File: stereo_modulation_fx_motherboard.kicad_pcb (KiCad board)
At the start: 2 copper layers, 101.6 x 139.7 mm, 87 parts, among them J1 dry_out_A, J10 Conn_01x04_Male, J11 Conn_01x04_Male, J12 Conn_01x04_Male, J13 Conn_01x02_Male, J14 Conn_01x02_Male, J2 CV_out_A, J3 wet_in_A, J4 rez_CV_out_A, J5 dry_out_B, J6 CV_out_B, J7 wet_in_B, J8 rez_CV_out_B, SW1 sweep_mode, SW2 invert_B, SW3 DPDT_on_on_on, U1 Teensy3.2, U10 DG419LDY, U11 DG419LDY, U2 CD74HC4067M, U3 MCP4822, U4 MCP4822, U5 TL072, U6 MCP6002-xSN, U7 TL072, U8 MCP6002-xSN, U9 CC3-0512DF-E

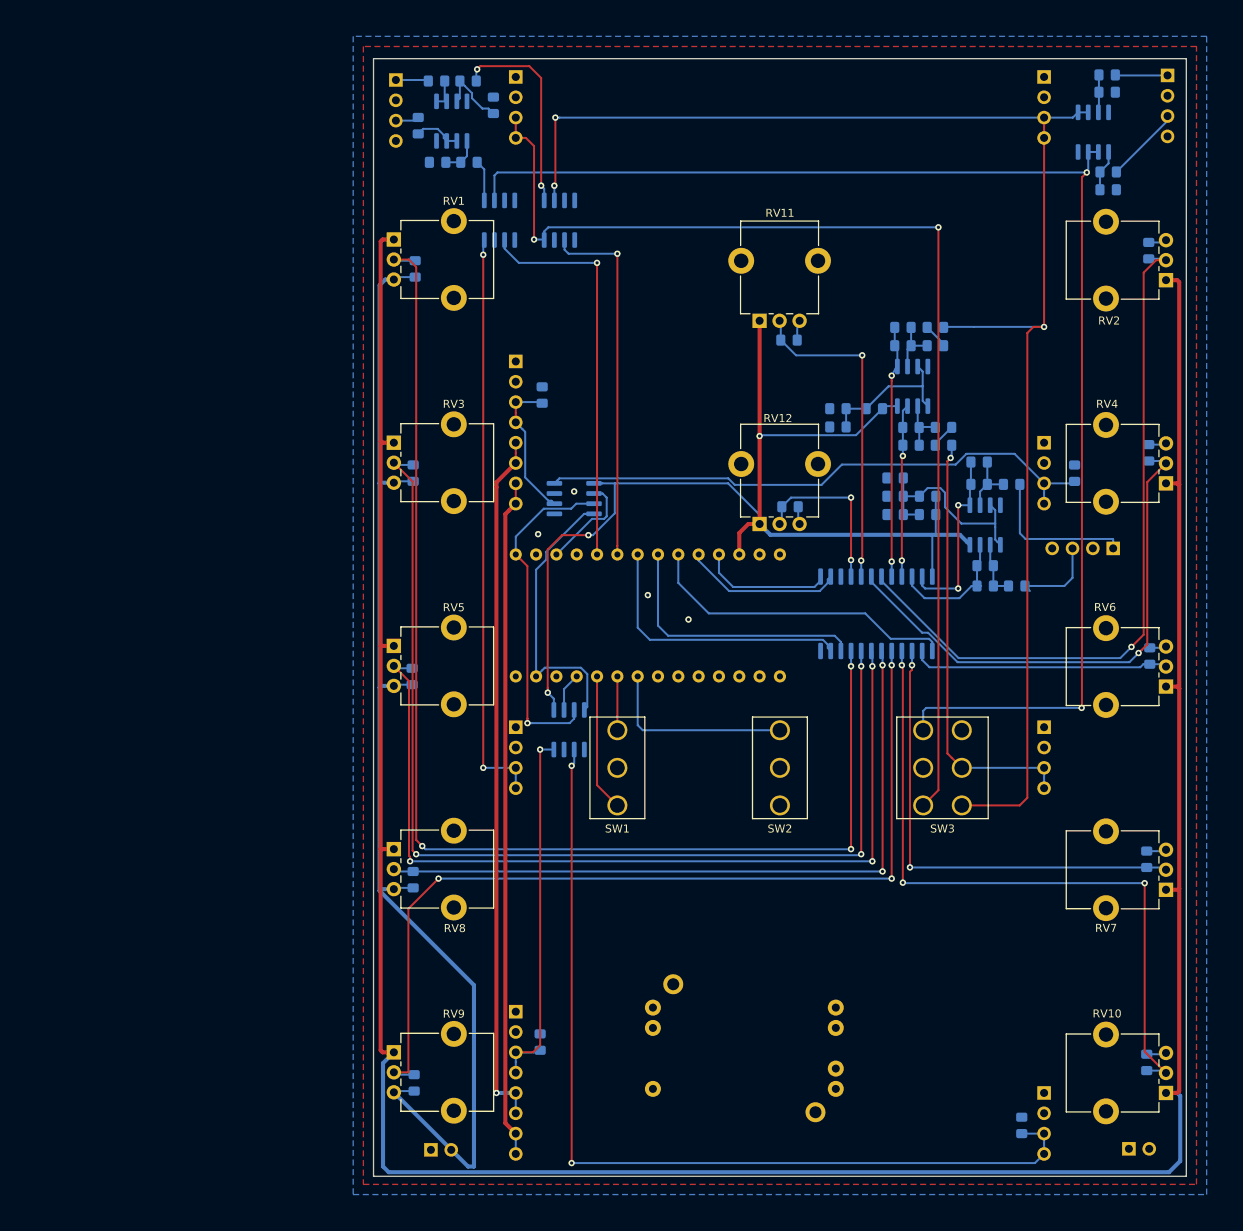
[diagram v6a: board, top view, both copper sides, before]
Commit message: move traces/vias away from pot tabs, progress on routing, NOT DONEgit add -A!
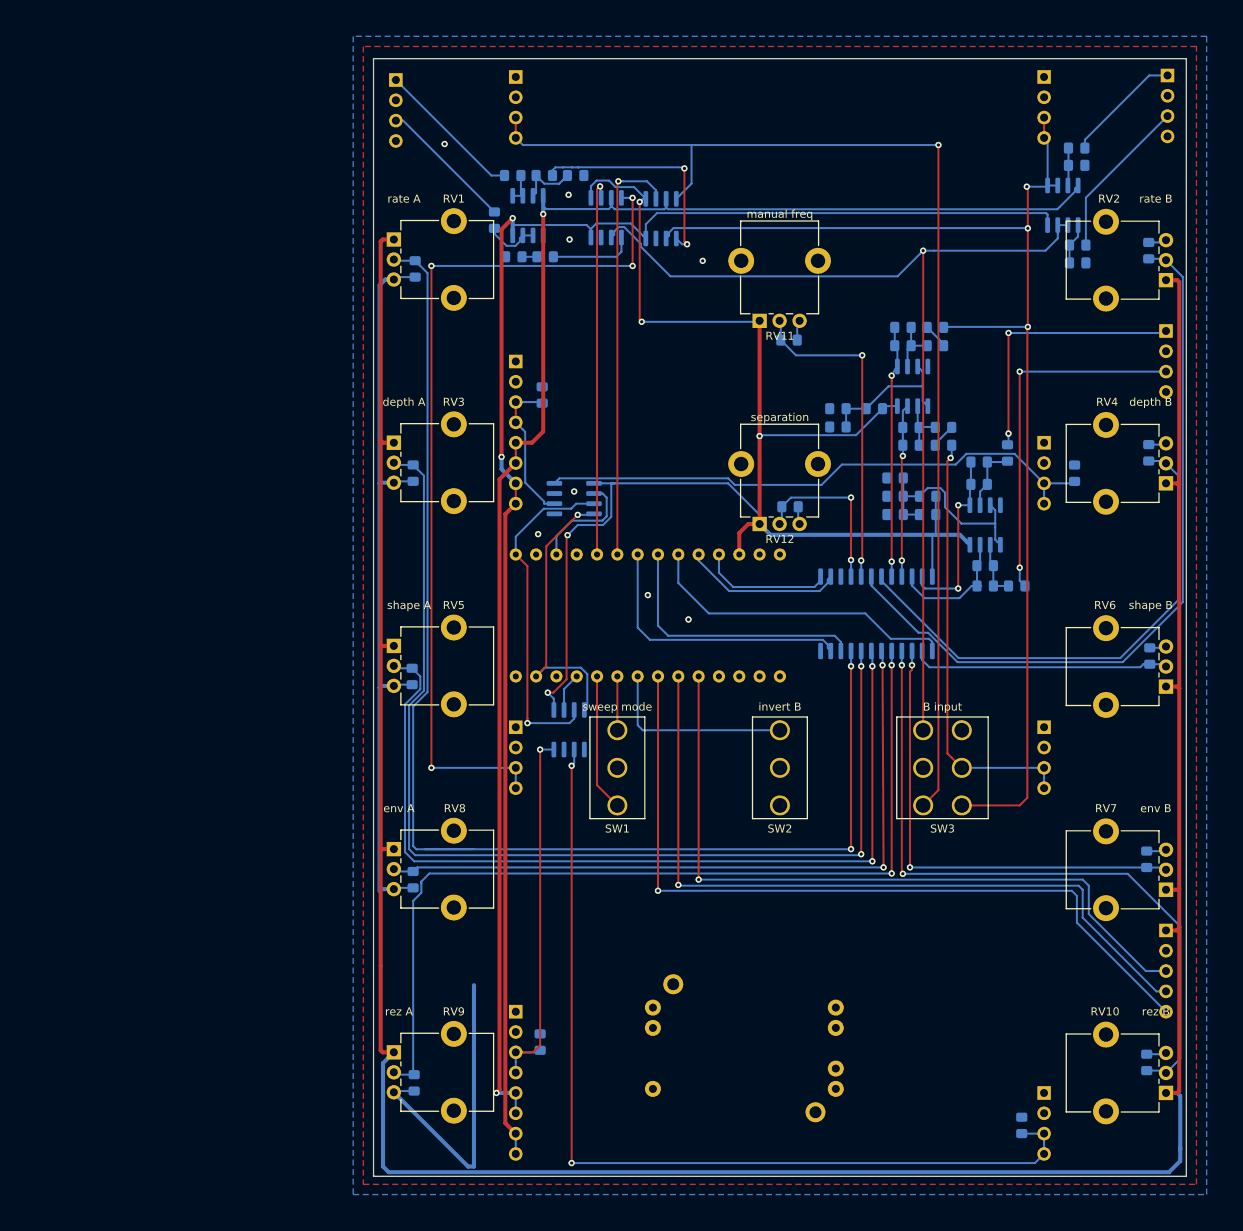
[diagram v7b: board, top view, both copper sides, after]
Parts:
- removed J14: Conn_01x02_Male, Connector_PinHeader_2.54mm:PinHeader_1x02_P2.54mm_Vertical
- J13: value Conn_01x02_Male -> Conn_01x05_Male; footprint Connector_PinHeader_2.54mm:PinHeader_1x02_P2.54mm_Vertical -> Connector_PinHeader_2.54mm:PinHeader_1x05_P2.54mm_Vertical
- moved J12 28.0 mm to (124.5, 59.7), turned to 180 degrees
- moved J13 27.7 mm to (124.5, 134.6), turned to 180 degrees
- moved R2 15.2 mm to (42.9, 50.4)
- moved C30 15.2 mm to (46.7, 40.3)
- moved C31 15.2 mm to (46.9, 50.4)
- moved R7 15.2 mm to (42.8, 40.3)
- moved R8 15.2 mm to (40.5, 45.8)
- moved U5 15.2 mm to (44.7, 45.3)
- moved R1 13.5 mm to (50.7, 40.3), turned to 0 degrees
- moved U11 13.3 mm to (54.5, 45.5), turned to 90 degrees
- moved U10 12.7 mm to (61.3, 45.7), turned to 90 degrees
- moved C27 9.91 mm to (113.4, 49.0)
- moved R6 9.91 mm to (113.4, 51.2)
- moved U7 9.91 mm to (111.6, 44.0)
- moved C26 9.91 mm to (113.3, 36.8)
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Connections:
- J13 pad 1: footswitch_A -> +3V3
- U1 pad 5: Net-(U1-Pad5) -> footswitch_A
- U1 pad 6: footswitch_A -> footswitch_B
- U1 pad 7: footswitch_B -> LED_serial
- U2 pad 18: depth_B -> rate_B
- U2 pad 19: rate_B -> depth_B
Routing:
- net +12V: track 84.9 -> 196.7 mm, vias 0 -> 2
- net -12V: track 87.2 -> 194.1 mm, vias 1 -> 2
- net LED_serial: track 0.00 -> 98.5 mm, vias 0 -> 1
- net footswitch_B: track 0.00 -> 94.6 mm, vias 0 -> 1
- net footswitch_A: track 0.00 -> 90.6 mm, vias 0 -> 1
- net Net-(SW3-Pad6): track 170.8 -> 124.2 mm, vias 2 -> 1
- net +3V3: track 490.1 -> 532.9 mm, vias 3 -> 5
- net wet_B: track 72.6 -> 110.9 mm, vias 2 -> 4
- net freq_CV_in: track 10.9 -> 45.4 mm, vias 0 -> 2
- net dry_A: track 185.1 -> 154.6 mm
- net GNDA: track 165.4 -> 148.8 mm, vias 4 -> 8
- net LFO_rate_CV_in: track 19.2 -> 33.8 mm, vias 0 -> 2
- net output_A: track 4.11 -> 18.7 mm
- net output_B: track 2.96 -> 17.0 mm
- net input_B: track 9.63 -> 20.4 mm
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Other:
- board text added: "3.3V"
- board text added: "B input"
- board text added: "depth A"
- board text added: "depth B"
- board text added: "env A"
- board text added: "env B"
- board text added: "fs A"
- board text added: "fs B"
- board text added: "gnd"
- board text added: "invert B"
- board text added: "led tx"
- board text added: "manual freq"
- board text added: "out A"
- board text added: "out B"
- board text added: "rate A"
- board text added: "rate B"
- board text added: "rez A"
- board text added: "rez B"
- board text added: "separation"
- board text added: "shape A"
- board text added: "shape B"
- board text added: "sweep mode"
- board text added: "teensy 3.2"

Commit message: move schematic blocks around, add LEDs
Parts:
- added D1: NeoPixel_THT, LED_THT:LED_D5.0mm-4_RGB, F.Cu at (54.6, 154.2)
- added D2: NeoPixel_THT, LED_THT:LED_D5.0mm-4_RGB, F.Cu at (100.3, 154.2)
- J13: value Conn_01x05_Male -> Conn_01x03_Male; footprint Connector_PinHeader_2.54mm:PinHeader_1x05_P2.54mm_Vertical -> Connector_PinHeader_2.54mm:PinHeader_1x03_P2.54mm_Vertical
- moved C1 61.5 mm to (45.8, 148.6)
- moved C3 61.1 mm to (106.4, 159.0)
- moved J13 3.17 mm to (124.5, 137.8)
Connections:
- C1 pad 1: CV_out_B -> rez_CV_out_B
- C3 pad 1: rez_CV_out_B -> CV_out_B
- J13 pad 1: +3V3 -> GNDA
- J13 pad 2: GNDA -> footswitch_A
- J13 pad 3: footswitch_A -> footswitch_B
- U4 pad 6: CV_out_B -> rez_CV_out_B
- U4 pad 8: rez_CV_out_B -> CV_out_B
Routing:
- net LED_serial: track 98.5 -> 0.00 mm, vias 1 -> 0
- net footswitch_A: track 90.6 -> 88.8 mm
- net +3V3: track 532.9 -> 531.1 mm
- net footswitch_B: track 94.6 -> 92.9 mm
- net CV_out_B: track 116.7 -> 117.2 mm
- net rez_CV_out_B: vias 1 -> 2
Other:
- board text removed: "3.3V"
- board text removed: "led tx"
